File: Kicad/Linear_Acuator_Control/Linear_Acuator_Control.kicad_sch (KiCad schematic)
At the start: 10 parts, among them K1 RT42xAxx, K3 RT42xAxx, Q1 IRLZ44N, Q2 IRLZ44N, U1 ESP32-S3-DevKitC

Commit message: changed to male XT60 connector
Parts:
- L1, L2: footprint Connector_AMASS:AMASS_XT60PW-F_1x02_P7.20mm_Horizontal -> Connector_AMASS:AMASS_XT60PW-M_1x02_P7.20mm_Horizontal
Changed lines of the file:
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@@
 			)
 		)
-		(property "Footprint" "Connector_AMASS:AMASS_XT60PW-F_1x02_P7.20mm_Horizontal"
+		(property "Footprint" "Connector_AMASS:AMASS_XT60PW-M_1x02_P7.20mm_Horizontal"
 			(at 185.42 48.26 0)
 			(effects
@@
 			)
 		)
-		(property "Footprint" "Connector_AMASS:AMASS_XT60PW-F_1x02_P7.20mm_Horizontal"
+		(property "Footprint" "Connector_AMASS:AMASS_XT60PW-M_1x02_P7.20mm_Horizontal"
 			(at 234.95 48.26 0)
 			(effects

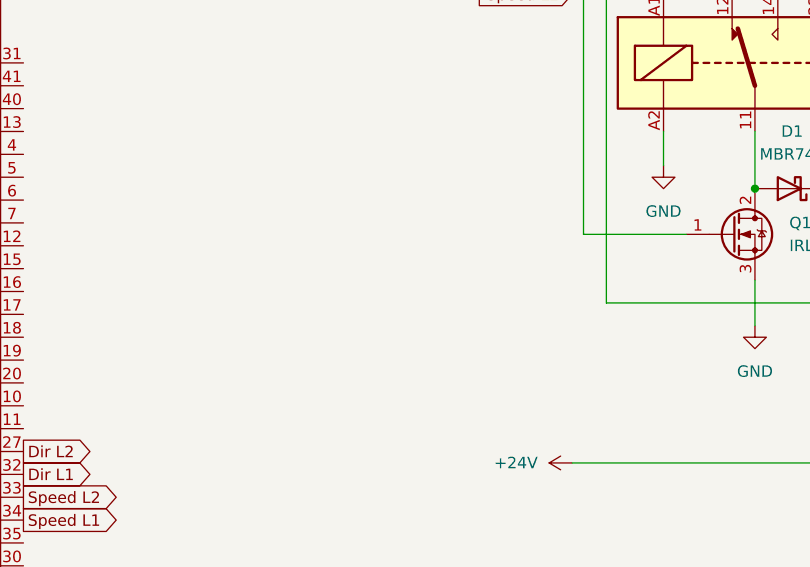
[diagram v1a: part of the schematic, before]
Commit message: Power input, minor rearranging
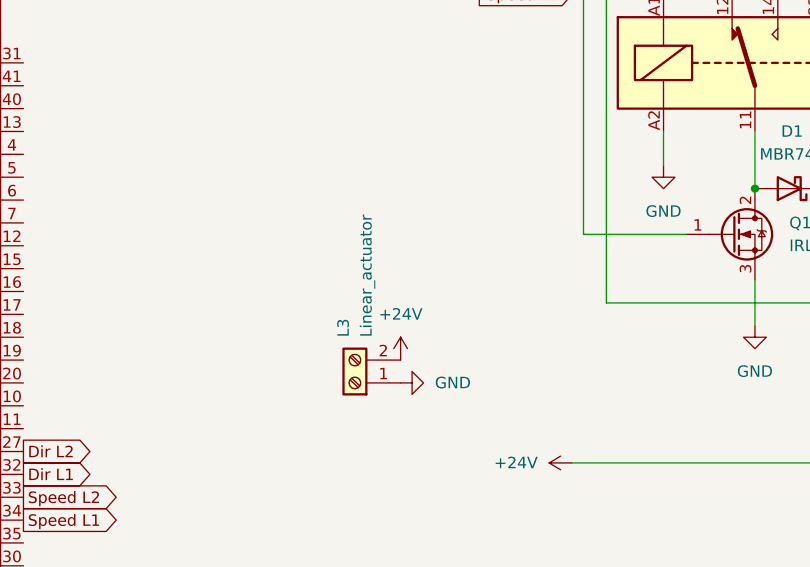
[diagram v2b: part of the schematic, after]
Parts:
- added L3: Linear_actuator, Connector_AMASS:AMASS_XT60PW-M_1x02_P7.20mm_Horizontal, symbol Connector:Screw_Terminal_01x02
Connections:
- net +24V: now also L3.2 (Pin_2)
- net GND: now also L3.1 (Pin_1)
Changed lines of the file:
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@@
+	)
+	(symbol
+		(lib_id "power:+24V")
+		(at 148.59 104.14 0)
+		(unit 1)
+		(exclude_from_sim no)
+		(in_bom yes)
+		(on_board yes)
+		(dnp no)
+		(fields_autoplaced yes)
+		(property "Reference" "#PWR09"
+			(at 148.59 107.95 0)
+			(effects
+				(font
+					(size 1.27 1.27)
+				)
+				(hide yes)
+			)
+		)
+		(property "Value" "+24V"
+			(at 148.59 99.06 0)
+			(effects
+				(font
+					(size 1.27 1.27)
+				)
+			)
+		)
+		(property "Footprint" ""
+			(at 148.59 104.14 0)
+			(effects
+				(font
+					(size 1.27 1.27)
+				)
+				(hide yes)
+			)
+		)
+		(property "Datasheet" ""
+			(at 148.59 104.14 0)
+			(effects
+				(font
+					(size 1.27 1.27)
+				)
+				(hide yes)
+			)
+		)
+		(property "Description" "Power symbol creates a global label with name \"+24V\""
+			(at 148.59 104.14 0)
+			(effects
+				(font
+					(size 1.27 1.27)
+				)
+				(hide yes)
+			)
+		)
+		(pin "1"
+		)
+		(instances
+			(project ""
+				(path "/f7047aaa-ba32-49d1-99b3-f492bbec601f"
+					(reference "#PWR09")
+					(unit 1)
+				)
+			)
+		)
 	)
 	(symbol
@@
 	(symbol
 		(lib_id "power:GND")
+		(at 148.59 106.68 90)
+		(unit 1)
+		(exclude_from_sim no)
+		(in_bom yes)
+		(on_board yes)
+		(dnp no)
+		(fields_autoplaced yes)
+		(property "Reference" "#PWR010"
+			(at 154.94 106.68 0)
+			(effects
+				(font
+					(size 1.27 1.27)
+				)
+				(hide yes)
+			)
+		)
+		(property "Value" "GND"
+			(at 152.4 106.6799 90)
+			(effects
+				(font
+					(size 1.27 1.27)
+				)
+				(justify right)
+			)
+		)
+		(property "Footprint" ""
+			(at 148.59 106.68 0)
+			(effects
+				(font
+					(size 1.27 1.27)
+				)
+				(hide yes)
+			)
+		)
+		(property "Datasheet" ""
+			(at 148.59 106.68 0)
+			(effects
+				(font
+					(size 1.27 1.27)
+				)
+				(hide yes)
+			)
+		)
+		(property "Description" "Power symbol creates a global label with name \"GND\" , ground"
+			(at 148.59 106.68 0)
+			(effects
+				(font
+					(size 1.27 1.27)
+				)
+				(hide yes)
+			)
+		)
+		(pin "1"
+		)
+		(instances
+			(project "Linear_Acuator_Control"
+				(path "/f7047aaa-ba32-49d1-99b3-f492bbec601f"
+					(reference "#PWR010")
+					(unit 1)
+				)
+			)
+		)
+	)
+	(symbol
+		(lib_id "power:GND")
 		(at 81.28 144.78 0)
 		(unit 1)
@@
 					(unit 1)
 				)
+			)
+		)
+	)
+	(symbol
+		(lib_id "Connector:Screw_Terminal_01x02")
+		(at 143.51 106.68 180)
+		(unit 1)
+		(exclude_from_sim no)
+		(in_bom yes)
+		(on_board yes)
+		(dnp no)
+		(property "Reference" "L3"
+			(at 142.2399 101.6 90)
+			(effects
+				(font
+					(size 1.27 1.27)
+				)
+				(justify right)
+			)
+		)
+		(property "Value" "Linear_actuator"
+			(at 144.7799 101.6 90)
+			(effects
+				(font
+					(size 1.27 1.27)
+				)
+				(justify right)
+			)
+		)
+		(property "Footprint" "Connector_AMASS:AMASS_XT60PW-M_1x02_P7.20mm_Horizontal"
+			(at 143.51 106.68 0)
+			(effects
+				(font
+					(size 1.27 1.27)
+				)
+				(hide yes)
+			)
+		)
+		(property "Datasheet" "~"
+			(at 143.51 106.68 0)
+			(effects
+				(font
+					(size 1.27 1.27)
+				)
+				(hide yes)
+			)
+		)
+		(property "Description" "Generic screw terminal, single row, 01x02, script generated (kicad-library-utils/schlib/autogen/connector/)"
+			(at 143.51 106.68 0)
+			(effects
+				(font
+					(size 1.27 1.27)
+				)
+				(hide yes)
+			)
+		)
+		(pin "1"
+		)
+		(pin "2"
+		)
+		(instances
+			(project "Linear_Acuator_Control"
+				(path "/f7047aaa-ba32-49d1-99b3-f492bbec601f"
+					(reference "L3")
+					(unit 1)
+				)
